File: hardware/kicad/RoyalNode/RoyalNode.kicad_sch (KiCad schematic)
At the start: 75 parts, among them J1 XT30PW-M SOLAR, J2 XT30PW-M BATTERY, J3 JST-GH XIAO BAT HARNESS, J4 JST-GH BATTERY NTC, J5 Molex 0732511150 SMA, Q1 ISA170170N04LMDS, Q2 ISA170170N04LMDS, Q3 ISA170170N04LMDS, U1 BQ25798RQMR, U2 LM66100DCKR, U3 TPS61088RHLR, U4 LTC4365ITS8-1

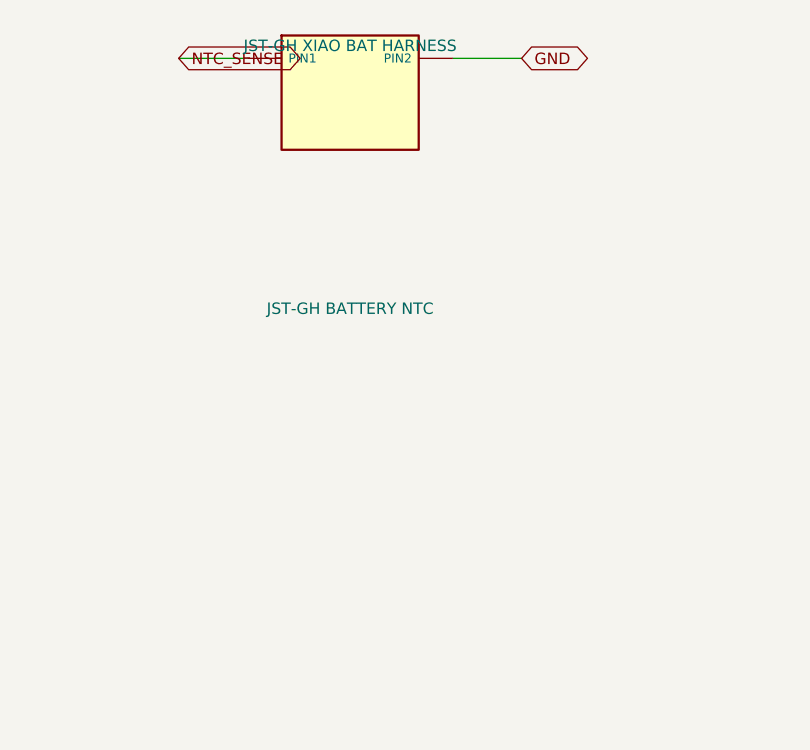
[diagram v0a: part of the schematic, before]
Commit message: Add optional BME680 I2C connector
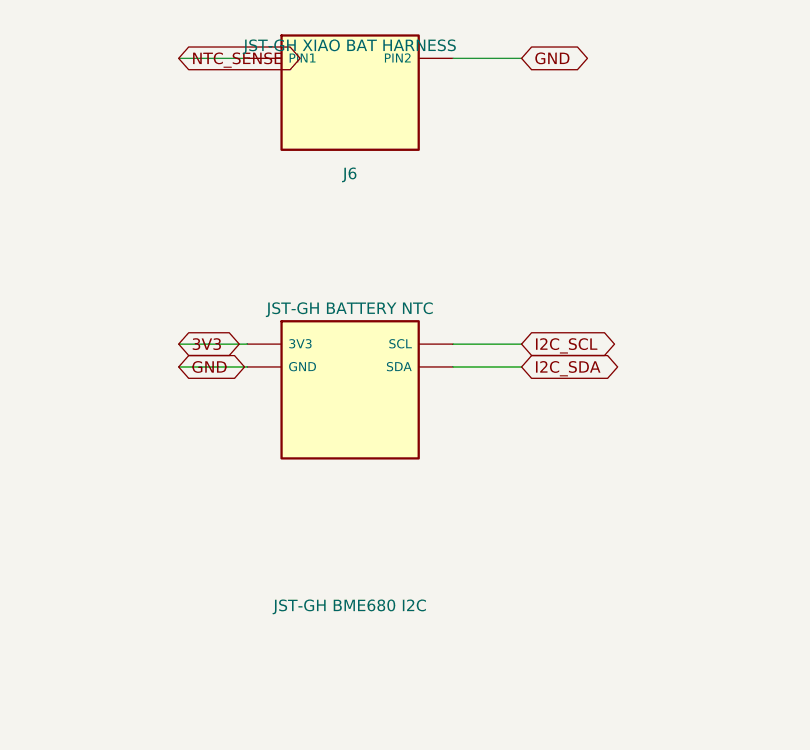
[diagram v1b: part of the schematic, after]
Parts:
- added J6: JST-GH BME680 I2C, RoyalNode:J_LOW_JST_GH_SM04B_GHS_TB_RC, symbol RoyalNode:RN_JST_GH_4
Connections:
- net 3V3: now also J6.1 (3V3)
- net GND: now also J6.2 (GND)
- net I2C_SCL: now also J6.4 (SCL)
- net I2C_SDA: now also J6.3 (SDA)
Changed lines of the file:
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@@
+  )
+  (symbol
+    (lib_id "RoyalNode:RN_JST_GH_4")
+    (at 149.86 266.70 0)
+    (unit 1)
+    (exclude_from_sim no)
+    (in_bom yes)
+    (on_board yes)
+    (dnp no)
+    (property "Reference" "J6"
+      (at 149.86 242.70 0)
+      (effects
+        (font
+          (size 1.27 1.27)
+        )
+      )
+    )
+    (property "Value" "JST-GH BME680 I2C"
+      (at 149.86 290.70 0)
+      (effects
+        (font
+          (size 1.27 1.27)
+        )
+      )
+    )
+    (property "Footprint" "RoyalNode:J_LOW_JST_GH_SM04B_GHS_TB_RC"
+      (at 149.86 266.70 0)
+      (effects
+        (font
+          (size 1.27 1.27)
+        )
+        (hide yes)
+      )
+    )
+    (property "Datasheet" "~"
+      (at 149.86 266.70 0)
+      (effects
+        (font
+          (size 1.27 1.27)
+        )
+        (hide yes)
+      )
+    )
+    (pin "1"
+    )
+    (pin "2"
+    )
+    (pin "3"
+    )
+    (pin "4"
+    )
+    (instances
+      (project "RoyalNode"
+        (path "/f3a7c64e-a7ea-5080-8843-d780f2c7a141"
+          (reference "J6")
+          (unit 1)
+        )
+      )
+    )
+  )
+  (wire
+    (pts
+      (xy 138.43 261.62)
+      (xy 130.81 261.62)
+    )
+    (stroke
+      (width 0)
+      (type default)
+    )
+  )
+  (global_label "3V3"
+    (shape bidirectional)
+    (at 130.81 261.62 180)
+    (fields_autoplaced yes)
+    (effects
+      (font
+        (size 1.27 1.27)
+      )
+      (justify left)
+    )
+    (property "Intersheetrefs" "${INTERSHEET_REFS}"
+      (at 130.81 261.62 180)
+      (effects
+        (font
+          (size 1.27 1.27)
+        )
+        (hide yes)
+      )
+    )
+  )
+  (wire
+    (pts
+      (xy 138.43 264.16)
+      (xy 130.81 264.16)
+    )
+    (stroke
+      (width 0)
+      (type default)
+    )
+  )
+  (global_label "GND"
+    (shape bidirectional)
+    (at 130.81 264.16 180)
+    (fields_autoplaced yes)
+    (effects
+      (font
+        (size 1.27 1.27)
+      )
+      (justify left)
+    )
+    (property "Intersheetrefs" "${INTERSHEET_REFS}"
+      (at 130.81 264.16 180)
+      (effects
+        (font
+          (size 1.27 1.27)
+        )
+        (hide yes)
+      )
+    )
+  )
+  (wire
+    (pts
+      (xy 161.29 264.16)
+      (xy 168.91 264.16)
+    )
+    (stroke
+      (width 0)
+      (type default)
+    )
+  )
+  (global_label "I2C_SDA"
+    (shape bidirectional)
+    (at 168.91 264.16 0)
+    (fields_autoplaced yes)
+    (effects
+      (font
+        (size 1.27 1.27)
+      )
+      (justify left)
+    )
+    (property "Intersheetrefs" "${INTERSHEET_REFS}"
+      (at 168.91 264.16 0)
+      (effects
+        (font
+          (size 1.27 1.27)
+        )
+        (hide yes)
+      )
+    )
+  )
+  (wire
+    (pts
+      (xy 161.29 261.62)
+      (xy 168.91 261.62)
+    )
+    (stroke
+      (width 0)
+      (type default)
+    )
+  )
+  (global_label "I2C_SCL"
+    (shape bidirectional)
+    (at 168.91 261.62 0)
+    (fields_autoplaced yes)
+    (effects
+      (font
+        (size 1.27 1.27)
+      )
+      (justify left)
+    )
+    (property "Intersheetrefs" "${INTERSHEET_REFS}"
+      (at 168.91 261.62 0)
+      (effects
+        (font
+          (size 1.27 1.27)
+        )
+        (hide yes)
+      )
+    )
   )
   (symbol

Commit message: Align solar input for 6V panel
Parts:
- F1: value Littelfuse 0483002.DR -> Littelfuse 0483005.DR
- R100: value 1.87 MOhm 1% -> 1.78 MOhm 1%
- R101: value 104 kOhm 0.1% -> 180 kOhm 0.1%
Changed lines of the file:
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@@
       )
     )
-    (property "Value" "Littelfuse 0483002.DR"
+    (property "Value" "Littelfuse 0483005.DR"
       (at 55.88 208.15 0)
       (effects
@@
       )
     )
-    (property "Value" "1.87 MOhm 1%"
+    (property "Value" "1.78 MOhm 1%"
       (at 335.28 59.56 0)
       (effects
@@
       )
     )
-    (property "Value" "104 kOhm 0.1%"
+    (property "Value" "180 kOhm 0.1%"
       (at 335.28 67.18 0)
       (effects

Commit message: Lock charge LED sourcing
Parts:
- D1: value Red 0603 LED -> KT-0603R red LED
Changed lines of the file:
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@@
       )
     )
-    (property "Value" "Red 0603 LED"
+    (property "Value" "KT-0603R red LED"
       (at 386.08 120.52 0)
       (effects

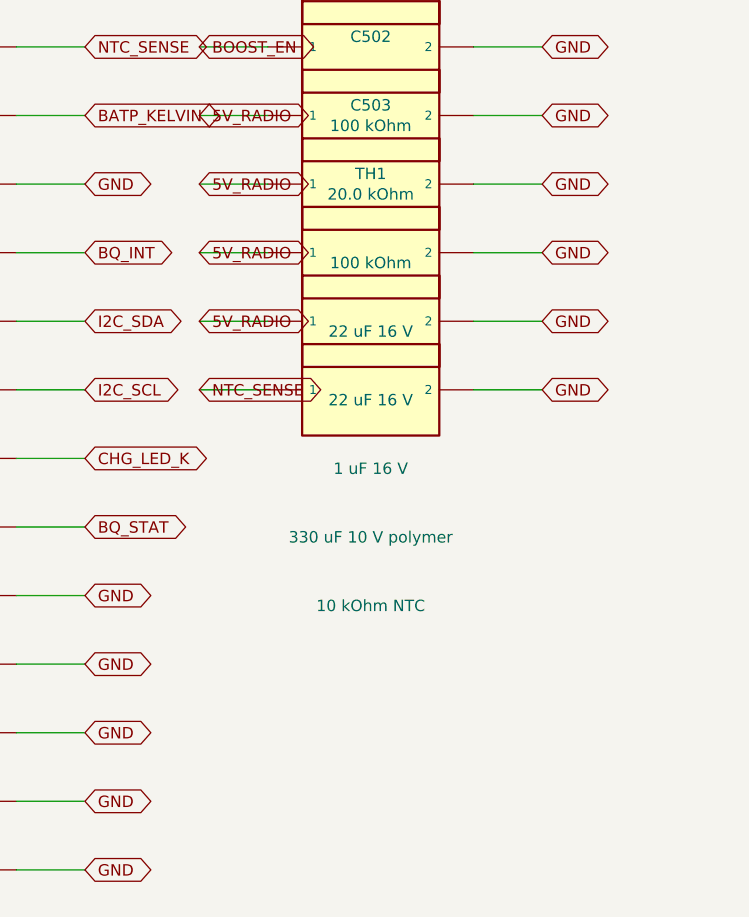
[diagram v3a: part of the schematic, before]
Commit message: Add E22 high frequency bypass caps
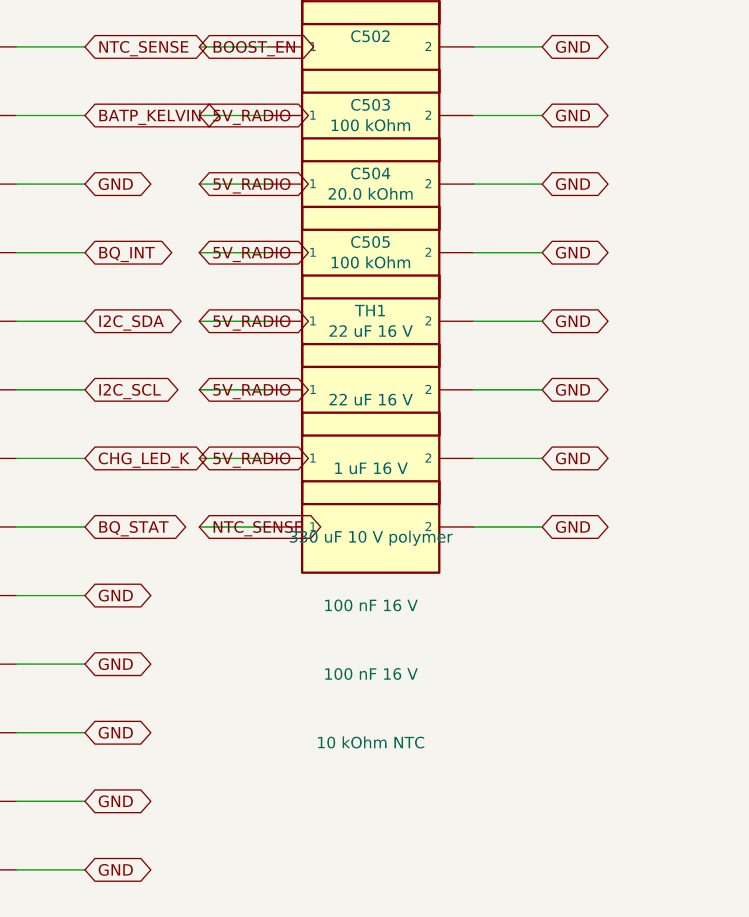
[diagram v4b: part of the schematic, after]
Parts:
- added C504, C505: 100 nF 16 V, Capacitor_SMD:C_0603_1608Metric, symbol RoyalNode:RN_TWO_PIN_POWER_PART
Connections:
- net 5V_RADIO: now also C504.1, C505.1
- net GND: now also C504.2, C505.2
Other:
- moved on the sheet: TH1
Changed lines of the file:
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@@
+    (exclude_from_sim no)
+    (in_bom yes)
+    (on_board yes)
+    (dnp no)
+    (property "Reference" "C504"
+      (at 436.88 64.90 0)
+      (effects
+        (font
+          (size 1.27 1.27)
+        )
+      )
+    )
+    (property "Value" "100 nF 16 V"
+      (at 436.88 112.90 0)
+      (effects
+        (font
+          (size 1.27 1.27)
+        )
+      )
+    )
+    (property "Footprint" "Capacitor_SMD:C_0603_1608Metric"
+      (at 436.88 88.90 0)
+      (effects
+        (font
+          (size 1.27 1.27)
+        )
+        (hide yes)
+      )
+    )
+    (property "Datasheet" "~"
+      (at 436.88 88.90 0)
+      (effects
+        (font
+          (size 1.27 1.27)
+        )
+        (hide yes)
+      )
+    )
+    (pin "1"
+    )
+    (pin "2"
+    )
+    (instances
+      (project "RoyalNode"
+        (path "/56bbf6bf-e8ee-572f-b29e-8187d12bd5fa"
+          (reference "C504")
+          (unit 1)
+        )
+      )
+    )
+  )
+  (wire
+    (pts
+      (xy 425.45 88.90)
+      (xy 417.83 88.90)
+    )
+    (stroke
+      (width 0)
+      (type default)
+    )
+  )
+  (global_label "5V_RADIO"
+    (shape bidirectional)
+    (at 417.83 88.90 180)
+    (fields_autoplaced yes)
+    (effects
+      (font
+        (size 1.27 1.27)
+      )
+      (justify left)
+    )
+    (property "Intersheetrefs" "${INTERSHEET_REFS}"
+      (at 417.83 88.90 180)
+      (effects
+        (font
+          (size 1.27 1.27)
+        )
+        (hide yes)
+      )
+    )
+  )
+  (wire
+    (pts
+      (xy 448.31 88.90)
+      (xy 455.93 88.90)
+    )
+    (stroke
+      (width 0)
+      (type default)
+    )
+  )
+  (global_label "GND"
+    (shape bidirectional)
+    (at 455.93 88.90 0)
+    (fields_autoplaced yes)
+    (effects
+      (font
+        (size 1.27 1.27)
+      )
+      (justify left)
+    )
+    (property "Intersheetrefs" "${INTERSHEET_REFS}"
+      (at 455.93 88.90 0)
+      (effects
+        (font
+          (size 1.27 1.27)
+        )
+        (hide yes)
+      )
+    )
+  )
+  (symbol
+    (lib_id "RoyalNode:RN_TWO_PIN_POWER_PART")
+    (at 436.88 96.52 0)
+    (unit 1)
+    (exclude_from_sim no)
+    (in_bom yes)
+    (on_board yes)
+    (dnp no)
+    (property "Reference" "C505"
+      (at 436.88 72.52 0)
+      (effects
+        (font
+          (size 1.27 1.27)
+        )
+      )
+    )
+    (property "Value" "100 nF 16 V"
+      (at 436.88 120.52 0)
+      (effects
+        (font
+          (size 1.27 1.27)
+        )
+      )
+    )
+    (property "Footprint" "Capacitor_SMD:C_0603_1608Metric"
+      (at 436.88 96.52 0)
+      (effects
+        (font
+          (size 1.27 1.27)
+        )
+        (hide yes)
+      )
+    )
+    (property "Datasheet" "~"
+      (at 436.88 96.52 0)
+      (effects
+        (font
+          (size 1.27 1.27)
+        )
+        (hide yes)
+      )
+    )
+    (pin "1"
+    )
+    (pin "2"
+    )
+    (instances
+      (project "RoyalNode"
+        (path "/f51db70b-8f1d-51f2-a3eb-b6a995a3532a"
+          (reference "C505")
+          (unit 1)
+        )
+      )
+    )
+  )
+  (wire
+    (pts
+      (xy 425.45 96.52)
+      (xy 417.83 96.52)
+    )
+    (stroke
+      (width 0)
+      (type default)
+    )
+  )
+  (global_label "5V_RADIO"
+    (shape bidirectional)
+    (at 417.83 96.52 180)
+    (fields_autoplaced yes)
+    (effects
+      (font
+        (size 1.27 1.27)
+      )
+      (justify left)
+    )
+    (property "Intersheetrefs" "${INTERSHEET_REFS}"
+      (at 417.83 96.52 180)
+      (effects
+        (font
+          (size 1.27 1.27)
+        )
+        (hide yes)
+      )
+    )
+  )
+  (wire
+    (pts
+      (xy 448.31 96.52)
+      (xy 455.93 96.52)
+    )
+    (stroke
+      (width 0)
+      (type default)
+    )
+  )
+  (global_label "GND"
+    (shape bidirectional)
+    (at 455.93 96.52 0)
+    (fields_autoplaced yes)
+    (effects
+      (font
+        (size 1.27 1.27)
+      )
+      (justify left)
+    )
+    (property "Intersheetrefs" "${INTERSHEET_REFS}"
+      (at 455.93 96.52 0)
+      (effects
+        (font
+          (size 1.27 1.27)
+        )
+        (hide yes)
+      )
+    )
+  )
+  (symbol
+    (lib_id "RoyalNode:RN_TWO_PIN_POWER_PART")
+    (at 436.88 104.14 0)
+    (unit 1)
     (exclude_from_sim no)
     (in_bom yes)
@@
     (dnp no)
     (property "Reference" "TH1"
-      (at 436.88 64.90 0)
+      (at 436.88 80.14 0)
       (effects
         (font
@@
     )
     (property "Value" "10 kOhm NTC"
-      (at 436.88 112.90 0)
+      (at 436.88 128.14 0)
       (effects
         (font
@@
     )
     (property "Footprint" ""
-      (at 436.88 88.90 0)
+      (at 436.88 104.14 0)
       (effects
         (font
@@
     )
     (property "Datasheet" "~"
-      (at 436.88 88.90 0)
+      (at 436.88 104.14 0)
       (effects
         (font
@@
   (wire
     (pts
-      (xy 425.45 88.90)
-      (xy 417.83 88.90)
+      (xy 425.45 104.14)
+      (xy 417.83 104.14)
     )
     (stroke
@@
   (global_label "NTC_SENSE"
     (shape bidirectional)
-    (at 417.83 88.90 180)
-    (fields_autoplaced yes)
-    (effects
-      (font
-        (size 1.27 1.27)
-      )
-      (justify left)
-    )
-    (property "Intersheetrefs" "${INTERSHEET_REFS}"
-      (at 417.83 88.90 180)
-      (effects
-        (font
-          (size 1.27 1.27)
-        )
-        (hide yes)
-      )
-    )
-  )
-  (wire
-    (pts
-      (xy 448.31 88.90)
-      (xy 455.93 88.90)
+    (at 417.83 104.14 180)
+    (fields_autoplaced yes)
+    (effects
+      (font
+        (size 1.27 1.27)
+      )
+      (justify left)
+    )
+    (property "Intersheetrefs" "${INTERSHEET_REFS}"
+      (at 417.83 104.14 180)
+      (effects
+        (font
+          (size 1.27 1.27)
+        )
+        (hide yes)
+      )
+    )
+  )
+  (wire
+    (pts
+      (xy 448.31 104.14)
+      (xy 455.93 104.14)
     )
     (stroke
@@
   (global_label "GND"
     (shape bidirectional)
-    (at 455.93 88.90 0)
-    (fields_autoplaced yes)
-    (effects
-      (font
-        (size 1.27 1.27)
-      )
-      (justify left)
-    )
-    (property "Intersheetrefs" "${INTERSHEET_REFS}"
-      (at 455.93 88.90 0)
-      (effects
-        (font
+    (at 455.93 104.14 0)
+    (fields_autoplaced yes)
+    (effects
+      (font
+        (size 1.27 1.27)
+      )
+      (justify left)
+    )
+    (property "Intersheetrefs" "${INTERSHEET_REFS}"
+      (at 455.93 104.14 0)
+      (effects
+        (font
